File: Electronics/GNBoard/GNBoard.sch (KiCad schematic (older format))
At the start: 14 parts, among them P1 Battery, SW1 PowerSwitch, U1 LM2576

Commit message: LDR and IR connectors added to schematic
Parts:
- added K?: IR1, ~, symbol CONN_3
- added K?: IR2, ~, symbol CONN_3
- added P2: CONN_5, ~, symbol CONN_5
- added R6, R7, R8, R9: 33k, ~, symbol R
- R1, R5: value R -> 6k8
- R2, R3, R4: value R -> 330
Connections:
- net +5V: now also K?.3 (P3), K?.3 (P3), R6.2, R7.2, R8.2, R9.2
- net GND: now also K?.2 (PM), K?.2 (PM), P2.1
- new net LDR1: P2.2, R9.1
- new net LDR2: P2.3, R8.1
- new net LDR3: P2.4, R7.1
- new net LDR4: P2.5, R6.1
- new net V_IR1: K?.1 (P1)
- new net V_IR2: K?.1 (P1)
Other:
- note added: "IR distance sensor connector"
- note added: "LDR connector"
- note added: "Power Switch"
- note added: "Servo connector"
- moved on the sheet: C1, C2, D1, L1, LED1, P1, R1, R2, R3, R4, R5, SW1A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

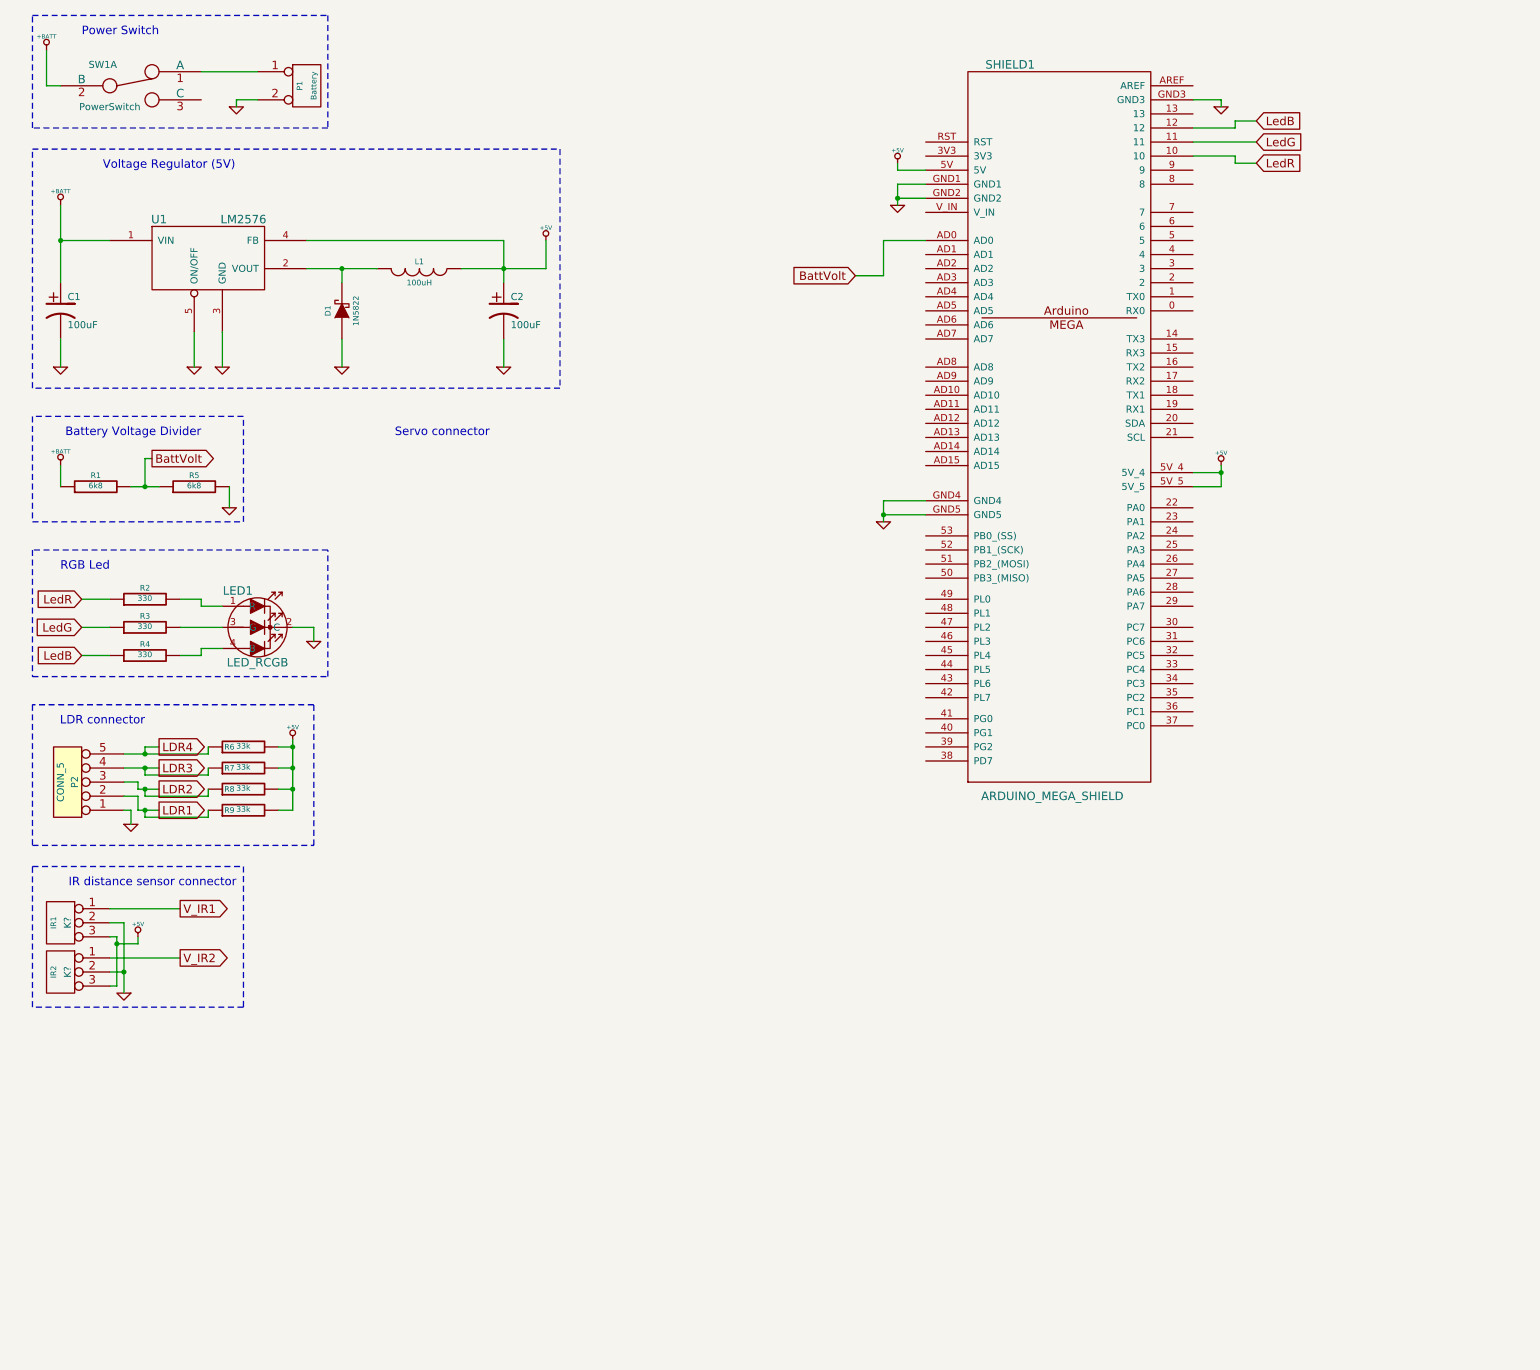
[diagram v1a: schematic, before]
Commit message: Layout for the LDR
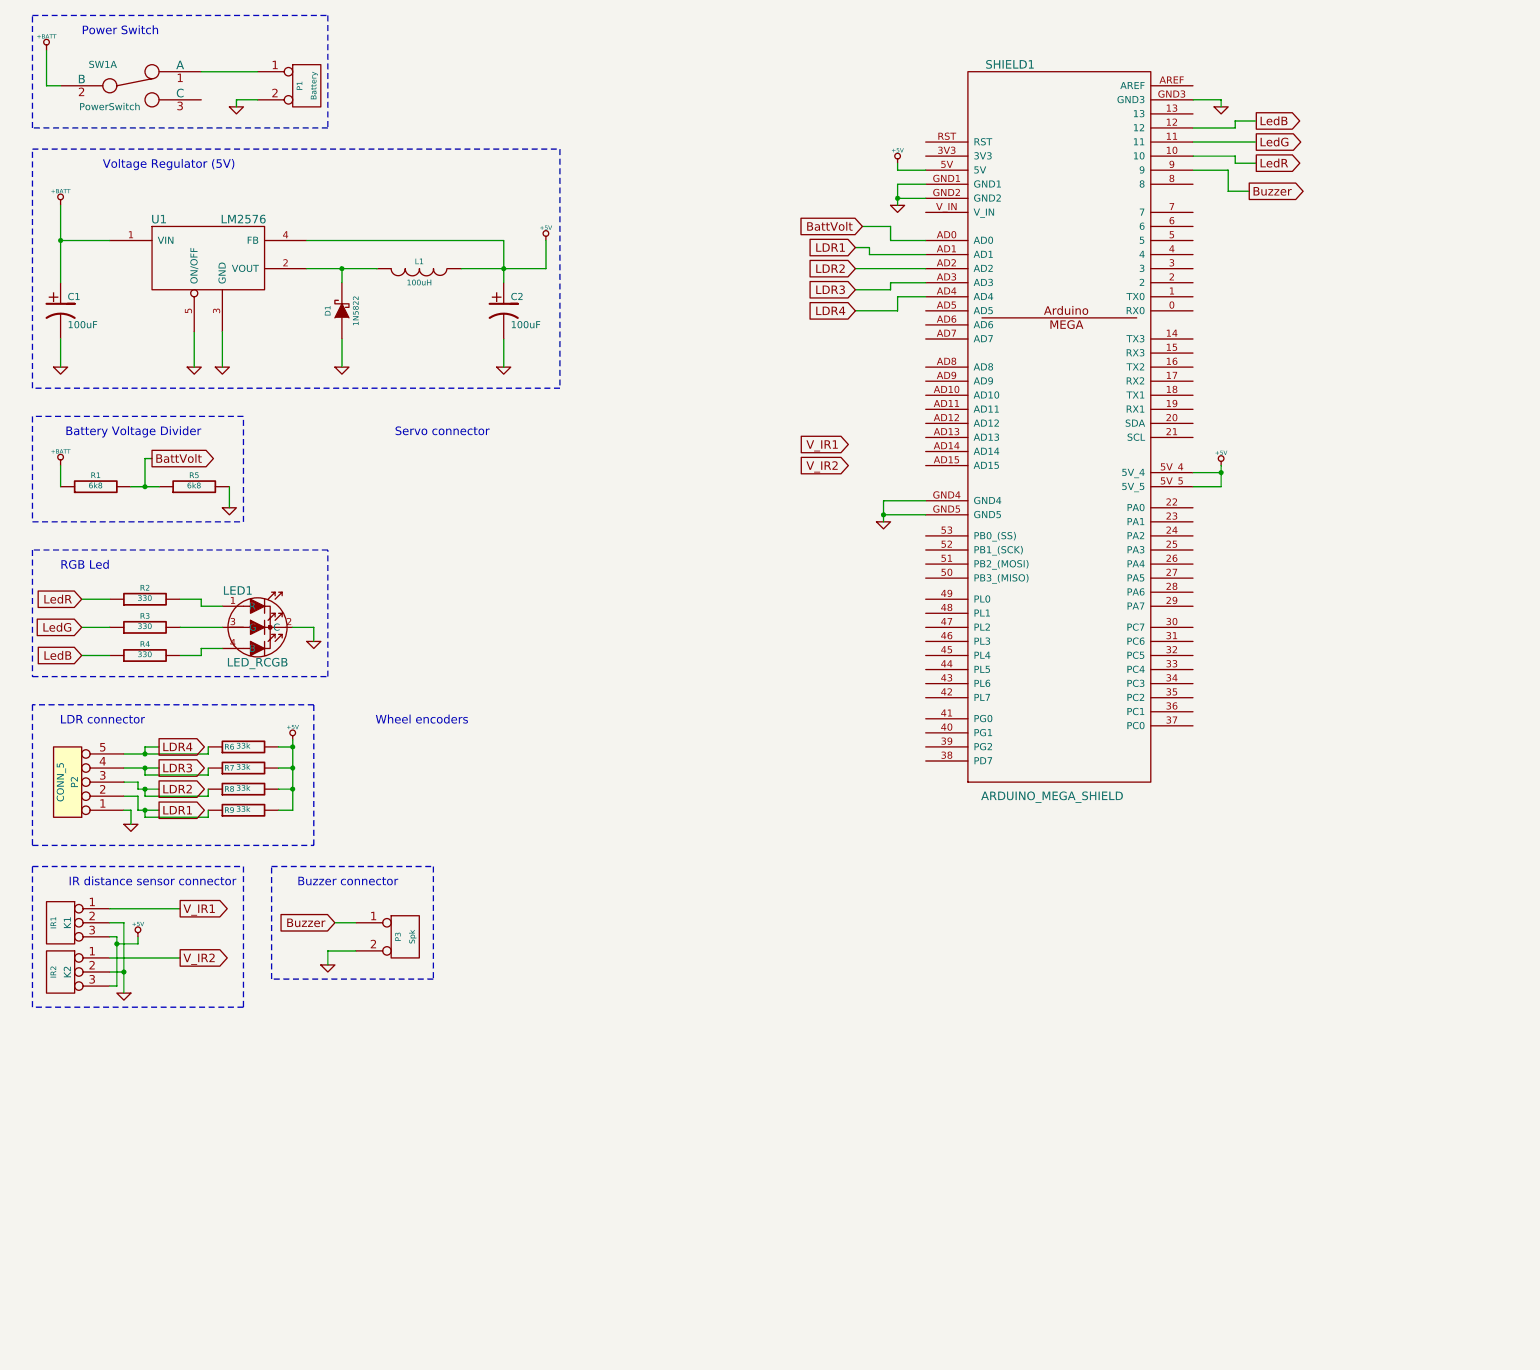
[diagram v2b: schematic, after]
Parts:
- added P3: Spk, ~, symbol CONN_2
- gave numbers to parts that had none: 2
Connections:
- net GND: now also P3.2 (PM)
- net LDR1: now also SHIELD1.AD1
- net LDR2: now also SHIELD1.AD2
- net LDR3: now also SHIELD1.AD3
- net LDR4: now also SHIELD1.AD4
- net Buzzer: now reaches SHIELD1.9
- net Buzzer: now also P3.1 (P1)
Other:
- note added: "Buzzer connector"
- note added: "Wheel encoders"
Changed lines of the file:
@@
-EESchema Schematic File Version 2  date jue 13 jun 2013 00:18:14 CEST
+EESchema Schematic File Version 2  date jue 13 jun 2013 00:51:02 CEST
 LIBS:LED_RGB
 LIBS:vreg
@@
 $EndDescr
 $Comp
-L GND #PWR17
+L GND #PWR20
 U 1 1 51B85F37
 P 6750 2000
-F 0 "#PWR17" H 6750 2000 30  0001 C CNN
+F 0 "#PWR20" H 6750 2000 30  0001 C CNN
 F 1 "GND" H 6750 1930 30  0001 C CNN
 F 2 "" H 6750 2000 60  0001 C CNN
@@
 Voltage Regulator (5V)
 $Comp
-L +5V #PWR14
+L +5V #PWR17
 U 1 1 51B8535B
 P 4250 2250
-F 0 "#PWR14" H 4250 2340 20  0001 C CNN
+F 0 "#PWR17" H 4250 2340 20  0001 C CNN
 F 1 "+5V" H 4250 2340 30  0000 C CNN
 F 2 "" H 4250 2250 60  0001 C CNN
@@
 $EndComp
 $Comp
-L GND #PWR13
+L GND #PWR16
 U 1 1 51B852D0
 P 3950 3150
-F 0 "#PWR13" H 3950 3150 30  0001 C CNN
+F 0 "#PWR16" H 3950 3150 30  0001 C CNN
 F 1 "GND" H 3950 3080 30  0001 C CNN
 F 2 "" H 3950 3150 60  0001 C CNN
@@
 $EndComp
 $Comp
-L GND #PWR12
+L GND #PWR15
 U 1 1 51B852CE
 P 2800 3150
-F 0 "#PWR12" H 2800 3150 30  0001 C CNN
+F 0 "#PWR15" H 2800 3150 30  0001 C CNN
 F 1 "GND" H 2800 3080 30  0001 C CNN
 F 2 "" H 2800 3150 60  0001 C CNN
@@
 $EndComp
 $Comp
-L GND #PWR7
+L GND #PWR9
 U 1 1 51B852C1
 P 1950 3150
-F 0 "#PWR7" H 1950 3150 30  0001 C CNN
+F 0 "#PWR9" H 1950 3150 30  0001 C CNN
 F 1 "GND" H 1950 3080 30  0001 C CNN
 F 2 "" H 1950 3150 60  0001 C CNN
@@
 $EndComp
 $Comp
-L GND #PWR6
+L GND #PWR8
 U 1 1 51B852BE
 P 1750 3150
-F 0 "#PWR6" H 1750 3150 30  0001 C CNN
+F 0 "#PWR8" H 1750 3150 30  0001 C CNN
 F 1 "GND" H 1750 3080 30  0001 C CNN
 F 2 "" H 1750 3150 60  0001 C CNN
@@
 $EndComp
 $Comp
-L +5V #PWR16
+L +5V #PWR19
 U 1 1 51B8519F
 P 6750 1700
-F 0 "#PWR16" H 6750 1790 20  0001 C CNN
+F 0 "#PWR19" H 6750 1790 20  0001 C CNN
 F 1 "+5V" H 6750 1790 30  0000 C CNN
 F 2 "" H 6750 1700 60  0001 C CNN
@@
 $EndComp
 $Comp
-L GND #PWR9
+L GND #PWR11
 U 1 1 51B88CF0
 P 2050 1300
-F 0 "#PWR9" H 2050 1300 30  0001 C CNN
+F 0 "#PWR11" H 2050 1300 30  0001 C CNN
 F 1 "GND" H 2050 1230 30  0001 C CNN
 F 2 "" H 2050 1300 60  0000 C CNN
@@
 $EndComp
 $Comp
-L GND #PWR8
+L GND #PWR10
 U 1 1 51B88EFE
 P 2000 4150
-F 0 "#PWR8" H 2000 4150 30  0001 C CNN
+F 0 "#PWR10" H 2000 4150 30  0001 C CNN
 F 1 "GND" H 2000 4080 30  0001 C CNN
 F 2 "" H 2000 4150 60  0000 C CNN
@@
 Text GLabel 1450 3800 2    60   Output ~ 0
 BattVolt
-Text GLabel 6450 2500 0    60   Input ~ 0
+Text GLabel 6500 2150 0    60   Input ~ 0
 BattVolt
 $Comp
@@
 $EndComp
 $Comp
-L GND #PWR11
+L GND #PWR13
 U 1 1 51B89466
 P 2600 5100
-F 0 "#PWR11" H 2600 5100 30  0001 C CNN
+F 0 "#PWR13" H 2600 5100 30  0001 C CNN
 F 1 "GND" H 2600 5030 30  0001 C CNN
 F 2 "" H 2600 5100 60  0000 C CNN
@@
 Text Notes 1800 3650 2    60   ~ 0
 Battery Voltage Divider
-Text GLabel 9300 1700 2    60   Input ~ 0
+Text GLabel 9300 1700 2    60   Output ~ 0
 LedR
-Text GLabel 9300 1550 2    60   Input ~ 0
+Text GLabel 9300 1550 2    60   Output ~ 0
 LedG
-Text GLabel 9300 1400 2    60   Input ~ 0
+Text GLabel 9300 1400 2    60   Output ~ 0
 LedB
 $Comp
-L GND #PWR18
+L GND #PWR21
 U 1 1 51B89E47
 P 9050 1300
-F 0 "#PWR18" H 9050 1300 30  0001 C CNN
+F 0 "#PWR21" H 9050 1300 30  0001 C CNN
 F 1 "GND" H 9050 1230 30  0001 C CNN
 F 2 "" H 9050 1300 60  0000 C CNN
@@
 $EndComp
 $Comp
-L GND #PWR15
+L GND #PWR18
 U 1 1 51B8A1C5
 P 6650 4250
-F 0 "#PWR15" H 6650 4250 30  0001 C CNN
+F 0 "#PWR18" H 6650 4250 30  0001 C CNN
 F 1 "GND" H 6650 4180 30  0001 C CNN
 F 2 "" H 6650 4250 60  0000 C CNN
@@
 $EndComp
 $Comp
-L +5V #PWR19
+L +5V #PWR22
 U 1 1 51B8C810
 P 9050 3850
-F 0 "#PWR19" H 9050 3940 20  0001 C CNN
+F 0 "#PWR22" H 9050 3940 20  0001 C CNN
 F 1 "+5V" H 9050 3940 30  0000 C CNN
 F 2 "" H 9050 3850 60  0000 C CNN
@@
 $EndComp
 $Comp
-L +5V #PWR10
+L +5V #PWR12
 U 1 1 51B8F35B
 P 2450 5800
-F 0 "#PWR10" H 2450 5890 20  0001 C CNN
+F 0 "#PWR12" H 2450 5890 20  0001 C CNN
 F 1 "+5V" H 2450 5890 30  0000 C CNN
 F 2 "" H 2450 5800 60  0000 C CNN
@@
 Wire Wire Line
 	2600 5100 2600 5000
-Wire Wire Line
-	6650 2500 6450 2500
-Wire Wire Line
-	6650 2250 6650 2500
-Wire Wire Line
-	6950 2250 6650 2250
 Connection ~ 1400 4000
 Wire Wire Line
@@
 	2600 5550 600  5550
 $Comp
-L GND #PWR5
+L GND #PWR6
 U 1 1 51B8F3D9
 P 1300 6400
-F 0 "#PWR5" H 1300 6400 30  0001 C CNN
+F 0 "#PWR6" H 1300 6400 30  0001 C CNN
 F 1 "GND" H 1300 6330 30  0001 C CNN
 F 2 "" H 1300 6400 60  0000 C CNN
@@
 Servo connector
 $Comp
-L CONN_3 K?
+L CONN_3 K1
 U 1 1 51B907F8
 P 800 7100
-F 0 "K?" V 750 7100 50  0000 C CNN
+F 0 "K1" V 750 7100 50  0000 C CNN
 F 1 "IR1" V 850 7100 40  0000 C CNN
 F 2 "~" H 800 7100 60  0000 C CNN
@@
 $EndComp
 $Comp
-L CONN_3 K?
+L CONN_3 K2
 U 1 1 51B90807
 P 800 7450
-F 0 "K?" V 750 7450 50  0000 C CNN
+F 0 "K2" V 750 7450 50  0000 C CNN
 F 1 "IR2" V 850 7450 40  0000 C CNN
 F 2 "~" H 800 7450 60  0000 C CNN
@@
 	1150 7000 1650 7000
 $Comp
-L GND #PWR?
+L GND #PWR5
 U 1 1 51B90E61
 P 1250 7600
-F 0 "#PWR?" H 1250 7600 30  0001 C CNN
+F 0 "#PWR5" H 1250 7600 30  0001 C CNN
 F 1 "GND" H 1250 7530 30  0001 C CNN
 F 2 "" H 1250 7600 60  0000 C CNN
@@
 $EndComp
 $Comp
-L +5V #PWR?
+L +5V #PWR7
 U 1 1 51B90E70
 P 1350 7200
-F 0 "#PWR?" H 1350 7290 20  0001 C CNN
+F 0 "#PWR7" H 1350 7290 20  0001 C CNN
 F 1 "+5V" H 1350 7290 30  0000 C CNN
 F 2 "" H 1350 7200 60  0000 C CNN
@@
 Wire Notes Line
 	600  7700 600  6700
+Text Notes 3700 5700 2    60   ~ 0
+Wheel encoders
+Text Notes 3200 6850 2    60   ~ 0
+Buzzer connector
+$Comp
+L CONN_2 P3
+U 1 1 51B8FA82
+P 3250 7200
+F 0 "P3" V 3200 7200 40  0000 C CNN
+F 1 "Spk" V 3300 7200 40  0000 C CNN
+F 2 "~" H 3250 7200 60  0000 C CNN
+F 3 "~" H 3250 7200 60  0000 C CNN
+	1    3250 7200
+	1    0    0    -1
+$EndComp
+$Comp
+L GND #PWR14
+U 1 1 51B8FA96
+P 2700 7400
+F 0 "#PWR14" H 2700 7400 30  0001 C CNN
+F 1 "GND" H 2700 7330 30  0001 C CNN
+F 2 "" H 2700 7400 60  0000 C CNN
+F 3 "" H 2700 7400 60  0000 C CNN
+	1    2700 7400
+	1    0    0    -1
+$EndComp
+Text GLabel 2750 7100 0    60   Input ~ 0
+Buzzer
+Wire Wire Line
+	2900 7300 2700 7300
+Wire Wire Line
+	2700 7300 2700 7400
+Wire Wire Line
+	2900 7100 2750 7100
+Wire Notes Line
+	2300 6700 3450 6700
+Wire Notes Line
+	3450 6700 3450 7500
+Wire Notes Line
+	3450 7500 2300 7500
+Wire Notes Line
+	2300 7500 2300 6700
+Text GLabel 9250 1900 2    60   Output ~ 0
+Buzzer
+Wire Wire Line
+	8850 1750 9100 1750
+Wire Wire Line
+	9100 1750 9100 1900
+Wire Wire Line
+	9100 1900 9250 1900
+Text GLabel 6450 2300 0    60   Input ~ 0
+LDR1
+Text GLabel 6450 2450 0    60   Input ~ 0
+LDR2
+Text GLabel 6450 2600 0    60   Input ~ 0
+LDR3
+Text GLabel 6450 2750 0    60   Input ~ 0
+LDR4
+Text GLabel 6400 3700 0    60   Input ~ 0
+V_IR1
+Text GLabel 6400 3850 0    60   Input ~ 0
+V_IR2
+Wire Wire Line
+	6500 2150 6700 2150
+Wire Wire Line
+	6700 2150 6700 2250
+Wire Wire Line
+	6700 2250 6950 2250
+Wire Wire Line
+	6950 2350 6550 2350
+Wire Wire Line
+	6550 2350 6550 2300
+Wire Wire Line
+	6550 2300 6450 2300
+Wire Wire Line
+	6450 2450 6950 2450
+Wire Wire Line
+	6950 2550 6700 2550
+Wire Wire Line
+	6700 2550 6700 2600
+Wire Wire Line
+	6700 2600 6450 2600
+Wire Wire Line
+	6450 2750 6750 2750
+Wire Wire Line
+	6750 2750 6750 2650
+Wire Wire Line
+	6750 2650 6950 2650
 $EndSCHEMATC

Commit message: v0.1 finished
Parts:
- added K10: IR4, ~, symbol CONN_3
- added K11: CNY_1, ~, symbol CONN_3
- added K12: CNY_2, ~, symbol CONN_3
- added K13: CNY_3, ~, symbol CONN_3
- added K14: CNY_4, ~, symbol CONN_3
- added K15: CNY_5, ~, symbol CONN_3
- added K16: CNY_6, ~, symbol CONN_3
- added K3: SERVO_1, ~, symbol CONN_3
- added K4: SERVO_2, ~, symbol CONN_3
- added K5: SERVO_3, ~, symbol CONN_3
- added K6: SERVO_4, ~, symbol CONN_3
- added K7: SERVO_5, ~, symbol CONN_3
- added K8: SERVO_6, ~, symbol CONN_3
- added K9: IR3, ~, symbol CONN_3
- added P4: I2C_1, ~, symbol CONN_4
- added P5: I2C_2, ~, symbol CONN_4
- added P6: DHT_Conn, ~, symbol CONN_4
- added R10, R11: R, ~, symbol R
- added R12: 10k, ~, symbol R
- added SW2, SW3: SW_PUSH, ~, symbol SW_PUSH
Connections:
- net +5V: now also K10.3 (P3), K11.2 (PM), K12.2 (PM), K13.2 (PM), K14.2 (PM), K15.2 (PM), K16.2 (PM), K3.2 (PM), K4.2 (PM), K5.2 (PM), K6.2 (PM), K7.2 (PM), K8.2 (PM), K9.3 (P3), P4.1 (P1), P5.1 (P1), P6.1 (P1), R10.1, R11.1, R12.1
- net Buzzer: now also SHIELD1.8; no longer SHIELD1.9
- net GND: now also K10.2 (PM), K11.3 (P3), K12.3 (P3), K13.3 (P3), K14.3 (P3), K15.3 (P3), K16.3 (P3), K3.3 (P3), K4.3 (P3), K5.3 (P3), K6.3 (P3), K7.3 (P3), K8.3 (P3), K9.2 (PM), P4.2 (P2), P5.2 (P2), P6.4 (P4), SW2.1, SW3.1
- net LedB: now also SHIELD1.11; no longer SHIELD1.12
- net LedG: now also SHIELD1.10; no longer SHIELD1.11
- net LedR: now also SHIELD1.9; no longer SHIELD1.10
- net V_IR1: now also SHIELD1.AD5
- net V_IR2: now also SHIELD1.AD6
- net CNY1: now reaches SHIELD1.14 (TX3)
- net CNY1: now also K11.1 (P1)
- net CNY2: now reaches SHIELD1.15 (RX3)
- net CNY2: now also K12.1 (P1)
- net CNY3: now reaches SHIELD1.16 (TX2)
- net CNY3: now also K13.1 (P1)
- net CNY4: now reaches SHIELD1.17 (RX2)
- net CNY4: now also K14.1 (P1)
- net CNY5: now reaches SHIELD1.18 (TX1)
- net CNY5: now also K15.1 (P1)
- net CNY6: now reaches SHIELD1.19 (RX1)
- net CNY6: now also K16.1 (P1)
- net Servo6: now reaches SHIELD1.2
- net Servo6: now also K8.1 (P1)
- net I2C_SDA: now reaches SHIELD1.20 (SDA)
- net I2C_SDA: now also P4.4 (P4), P5.4 (P4), R11.2
- net I2C_SCL: now reaches SHIELD1.21 (SCL)
- net I2C_SCL: now also P4.3 (P3), P5.3 (P3), R10.2
- net Servo5: now reaches SHIELD1.3
- net Servo5: now also K7.1 (P1)
- net Servo4: now reaches SHIELD1.4
- net Servo4: now also K6.1 (P1)
- net Servo3: now reaches SHIELD1.5
- net Servo3: now also K5.1 (P1)
- net Servo2: now reaches SHIELD1.6
- net Servo2: now also K4.1 (P1)
- net Servo1: now reaches SHIELD1.7
- net Servo1: now also K3.1 (P1)
- net V_IR3: now reaches SHIELD1.AD7
- net V_IR3: now also K9.1 (P1)
- net V_IR4: now reaches SHIELD1.AD8
- net V_IR4: now also K10.1 (P1)
- net DHTpin: now reaches SHIELD1.AD9
- net DHTpin: now also P6.2 (P2), R12.2
- net ResetB: now reaches SHIELD1.RST
- net ResetB: now also SW3.2
- new net Button1: SHIELD1.12, SW2.2
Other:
- note added: "Button 1"
- note added: "CNY70 pins"
- note added: "I2C Bus"
- note added: "Reset button"
- note added: "Servo connectors"
- note added: "Temp. and Hum. sensor (DHT11)"
- note removed: "Servo connector"
- note removed: "Wheel encoders"
- moved on the sheet: K1, K2, P3, SHIELD1

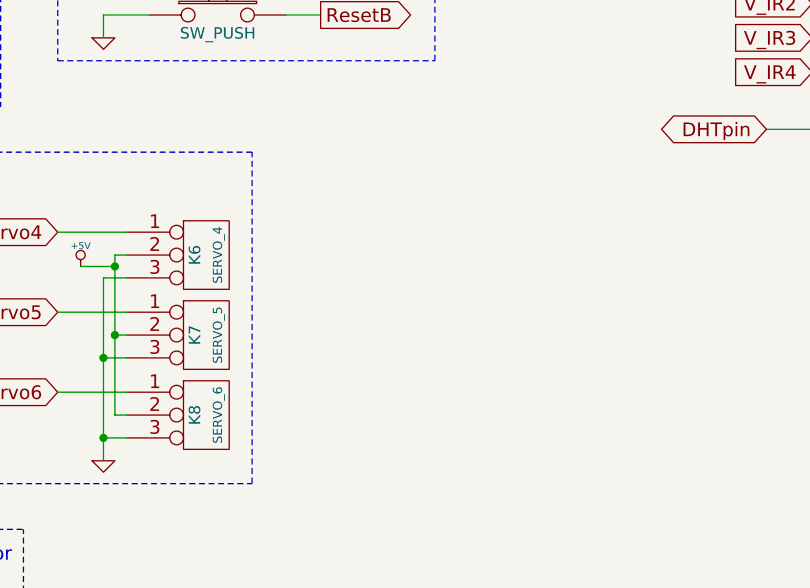
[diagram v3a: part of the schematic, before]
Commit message: Added decoupling caps
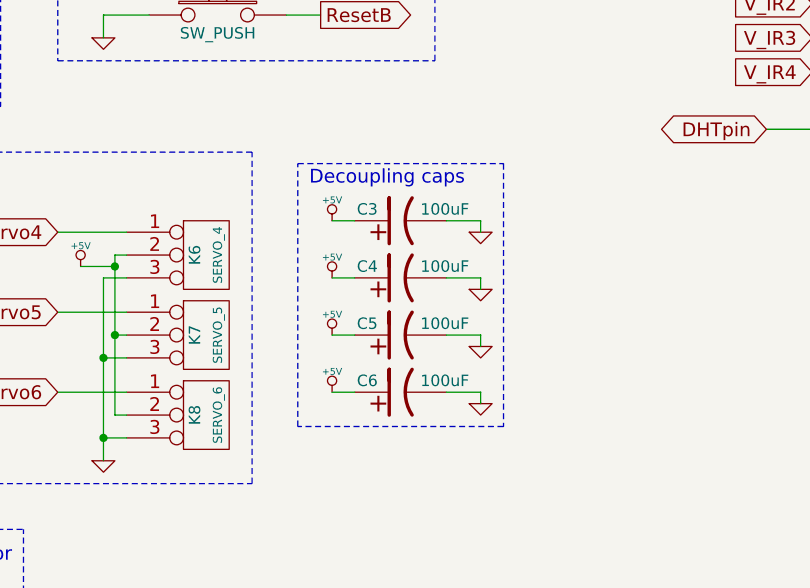
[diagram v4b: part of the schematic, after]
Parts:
- added C3, C4, C5, C6: 100uF, symbol CP1
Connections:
- net +5V: now also C3.1, C4.1, C5.1, C6.1
- net GND: now also C3.2, C4.2, C5.2, C6.2
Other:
- note added: "Decoupling caps"
